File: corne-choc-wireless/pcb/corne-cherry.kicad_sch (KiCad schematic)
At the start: 146 parts, among them J1 MJ-4PP-9, J2 OLED, J3 MJ-4PP-9, J4 OLED, SW1 SW_PUSH, SW10 SW_PUSH, SW11 SW_PUSH, SW12 SW_PUSH, SW13 SW_PUSH, SW14 SW_PUSH, SW15 SW_PUSH, SW16 SW_PUSH, SW17 SW_PUSH, SW18 SW_PUSH, SW19 SW_PUSH, SW2 SW_PUSH, SW20 SW_PUSH, SW21 SW_PUSH, SW22 SW_PUSH, SW23 SW_PUSH, SW24 SW_PUSH, SW25 SW_PUSH, SW26 SW_PUSH, SW27 SW_PUSH, SW29 SW_PUSH, SW3 SW_PUSH, SW30 SW_PUSH, SW31 SW_PUSH, SW32 SW_PUSH, SW33 SW_PUSH, SW34 SW_PUSH, SW35 SW_PUSH, SW36 SW_PUSH, SW37 SW_PUSH, SW38 SW_PUSH, SW39 SW_PUSH, SW4 SW_PUSH, SW40 SW_PUSH, SW41 SW_PUSH, SW42 SW_PUSH, SW5 SW_PUSH, SW6 SW_PUSH, SW8 SW_PUSH, SW9 SW_PUSH, U1 ProMicro, U2 ProMicro

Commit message: Wire up encoder
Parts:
- U1, U2: value ProMicro -> Nice!Nano; footprint kbd:ProMicro_v3 -> ScottoKeebs_MCU:Nice_Nano_V2; symbol kbd:ProMicro -> ScottoKeebs:MCU_Nice_Nano_V2
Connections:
- net GND: now also L_ENC.C
- net GNDA: now also R_ENC.C; no longer U2.23 (GND)
- net R_Enc_1: no longer U2.20 (F4/A3)
- net VDD: no longer U2.21 (VCC)
- net col1_r: no longer U2.19 (F5/A2)
- net col2_r: no longer U2.18 (F6/A1)
- net col3_r: no longer U2.17 (F7/A0)
- net col4_r: no longer U2.16 (B1/15)
- net col5_r: no longer U2.15 (B3/14)
- net reset_r: no longer U2.22 (RST)
- net L_ENC_B: now reaches U1.13 (D10)
- net L_ENC_B: now also L_ENC.B
- net L_ENC_A: now reaches U1.14 (D16)
- net L_ENC_A: now also L_ENC.A
- net R_ENC_A: now reaches R_ENC.A
- net R_ENC_B: now reaches R_ENC.B
- no-connect marks 14 -> 10
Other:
- moved on the sheet: D1, D10, D11, D12, D13, D14, D15, D16, D17, D18, D19, D2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

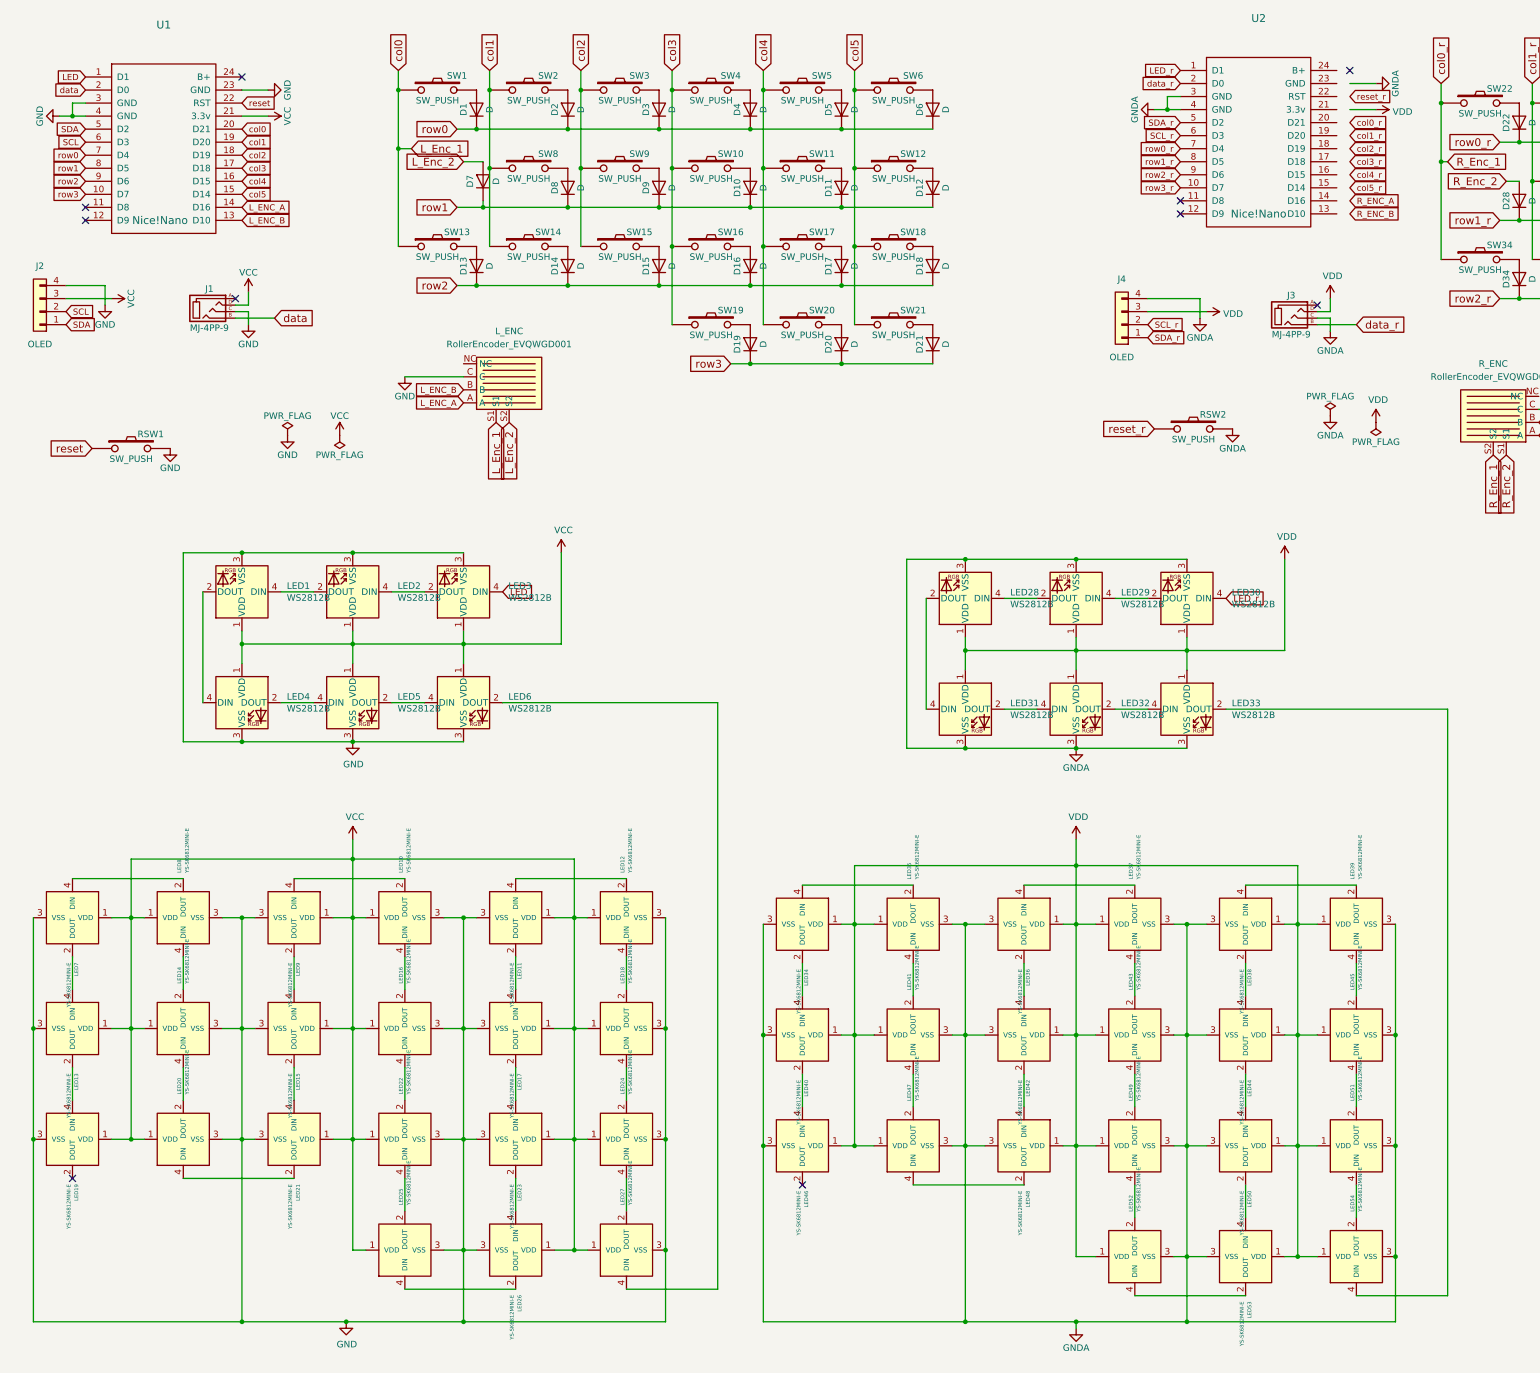
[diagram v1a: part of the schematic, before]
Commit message: Change to 5 pin for N!V
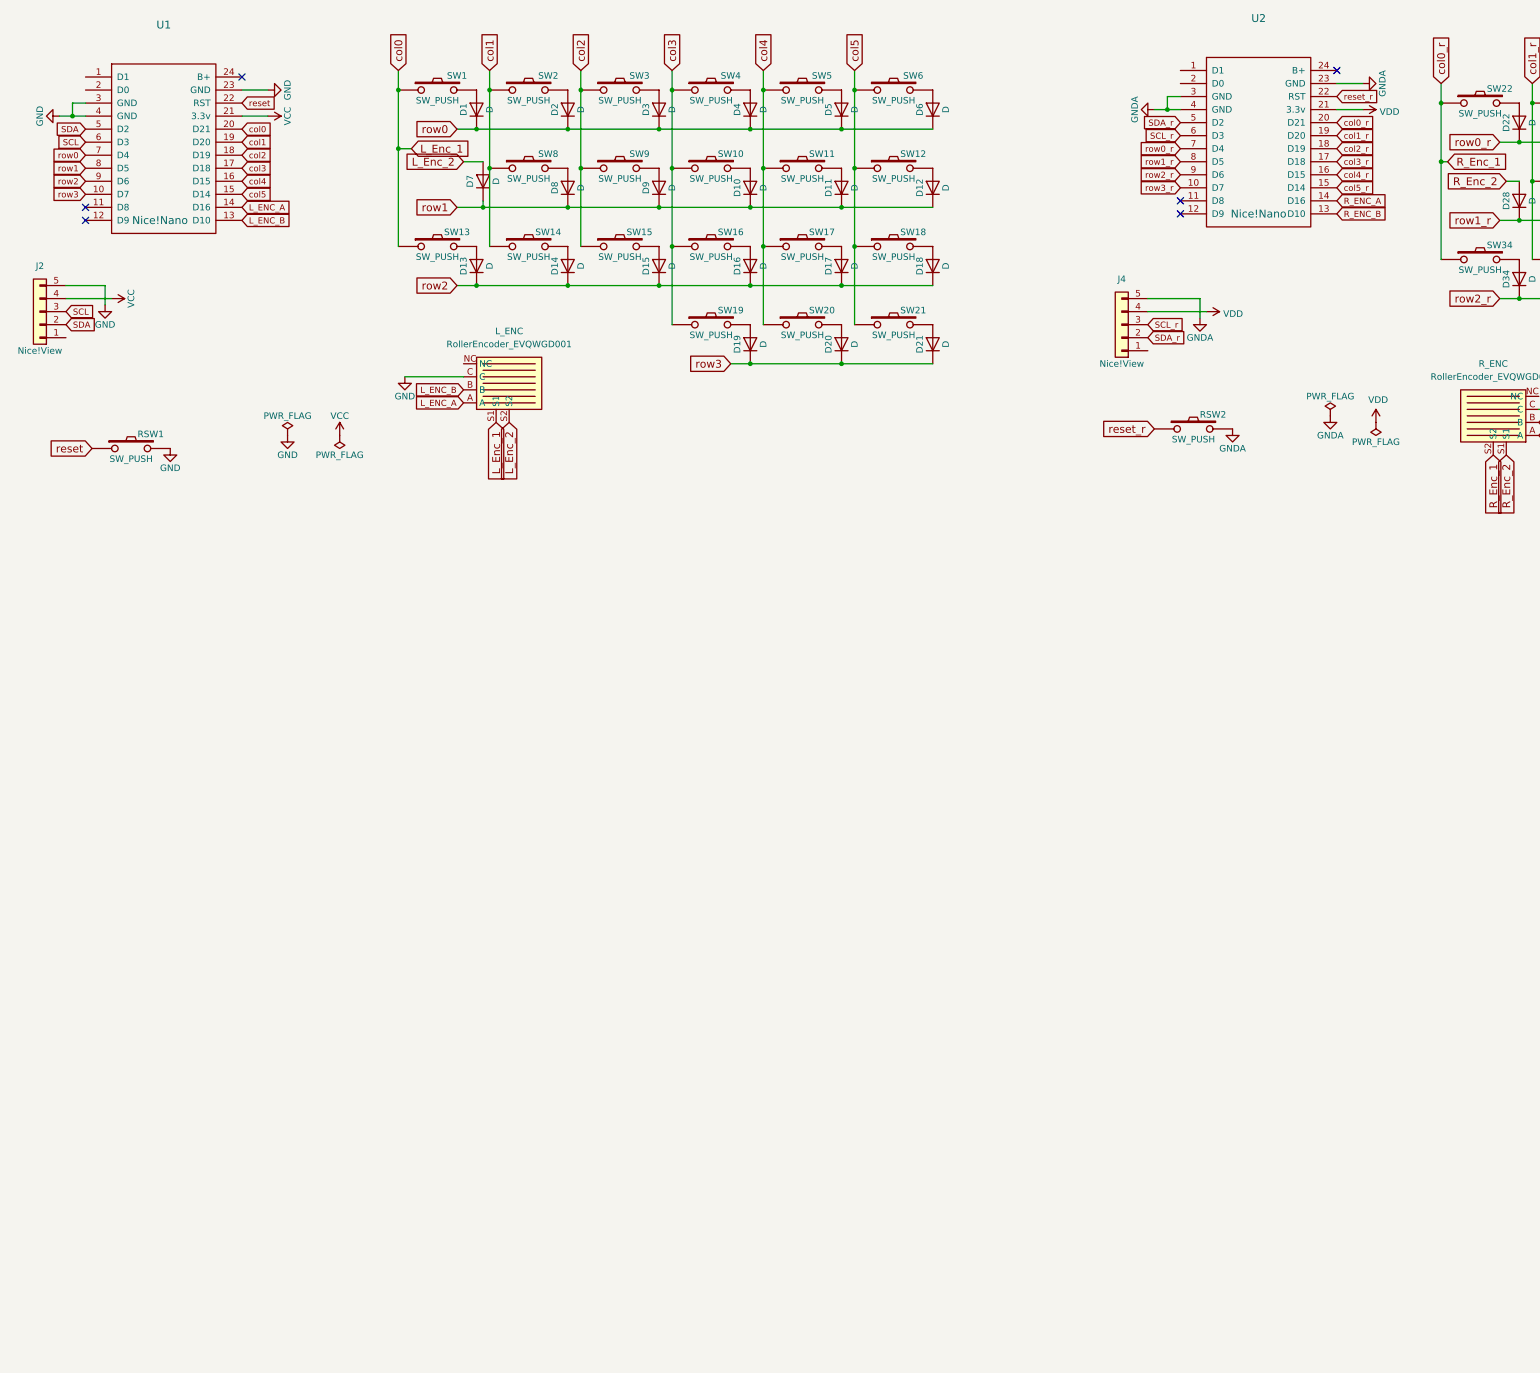
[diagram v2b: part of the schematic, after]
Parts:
- removed J1, J3: MJ-4PP-9, kbd:MJ-4PP-9_1side, symbol kbd:MJ-4PP-9
- removed LED1, LED2, LED28, LED29, LED3, LED30, LED31, LED32, LED33, LED4, LED5, LED6: WS2812B, LED_SMD:LED_WS2812B_PLCC4_5.0x5.0mm_P3.2mm, symbol LED:WS2812B
- removed LED10, LED11, LED12, LED13, LED14, LED15, LED16, LED17, LED18, LED19, LED20, LED21, LED22, LED23, LED24, LED25, LED26, LED27, LED34, LED35, LED36, LED37, LED38, LED39, LED40, LED41, LED42, LED43, LED44, LED45, LED46, LED47, LED48, LED49, LED50, LED51, LED52, LED53, LED54, LED7, LED8, LED9: YS-SK6812MINI-E, kbd:YS-SK6812MINI-E, symbol kbd:YS-SK6812MINI-E
- J2, J4: value OLED -> Nice!View; symbol Connector_Generic:Conn_01x04 -> Connector_Generic:Conn_01x05
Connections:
- net GND: now also J2.5 (Pin_5); no longer J2.4 (Pin_4)
- net GNDA: now also J4.5 (Pin_5), U2.23 (GND); no longer J4.4 (Pin_4)
- net R_ENC_A: now also U2.14 (D16)
- net R_ENC_B: now also U2.13 (D10)
- net R_Enc_1: now also U2.20 (D21)
- net SCL: now also J2.3 (Pin_3); no longer J2.2 (Pin_2)
- net SCL_r: now also J4.3 (Pin_3); no longer J4.2 (Pin_2)
- net SDA: now also J2.2 (Pin_2); no longer J2.1 (Pin_1)
- net SDA_r: now also J4.2 (Pin_2); no longer J4.1 (Pin_1)
- net VCC: now also J2.4 (Pin_4); no longer J2.3 (Pin_3)
- net VDD: now also J4.4 (Pin_4), U2.21 (3.3v); no longer J4.3 (Pin_3)
- net col1_r: now also U2.19 (D20)
- net col2_r: now also U2.18 (D19)
- net col3_r: now also U2.17 (D18)
- net col4_r: now also U2.16 (D15)
- net col5_r: now also U2.15 (D14)
- net reset_r: now also U2.22 (RST)
- net LED: no longer names the net of U1.1 (D1)
- net LED_r: no longer names the net of U2.1 (D1)
- net data: no longer names the net of U1.2 (D0)
- net data_r: no longer names the net of U2.2 (D0)
- no-connect marks 10 -> 6
